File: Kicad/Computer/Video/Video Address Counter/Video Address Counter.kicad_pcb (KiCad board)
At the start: 2 copper layers, 26.7 x 90.2 mm, 5 parts, among them IC1 AP7365-33WG-7, J1 Conn_02x32_Counter_Clockwise

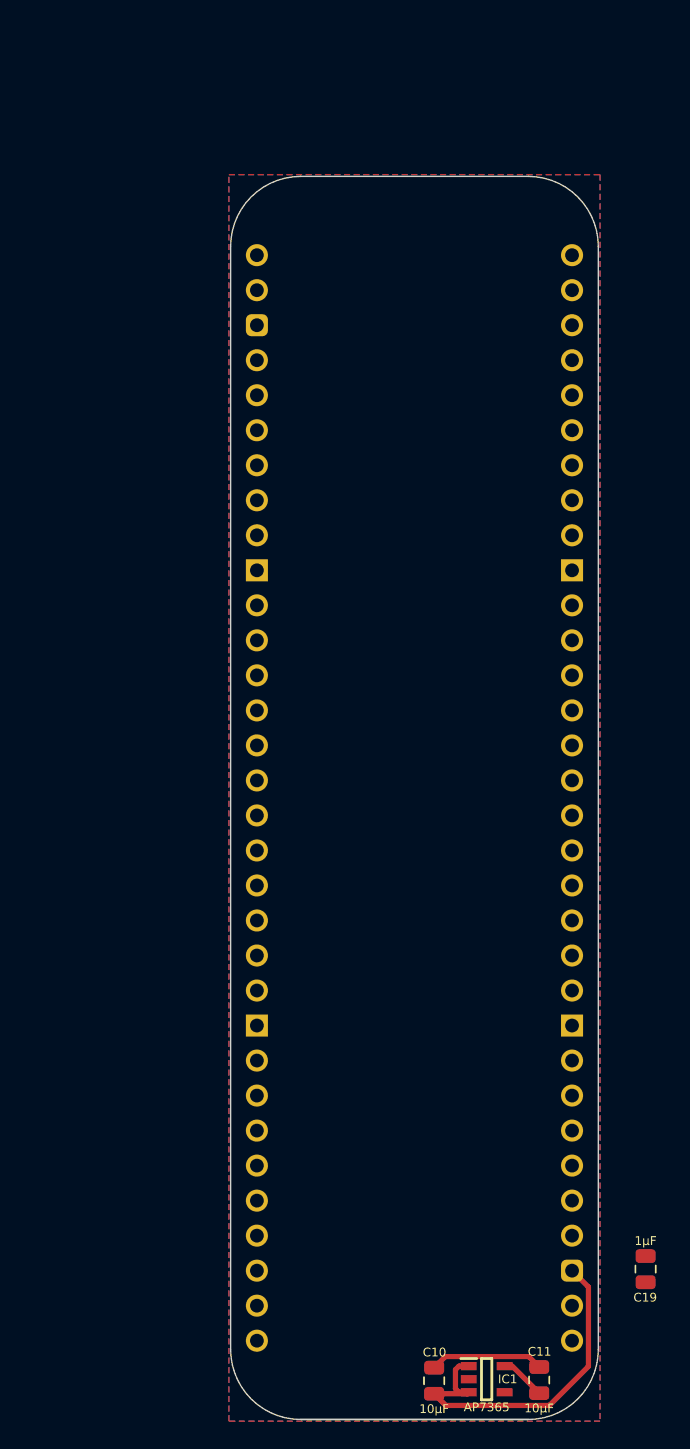
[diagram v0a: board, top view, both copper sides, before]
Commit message: Adding Video Address Counter.
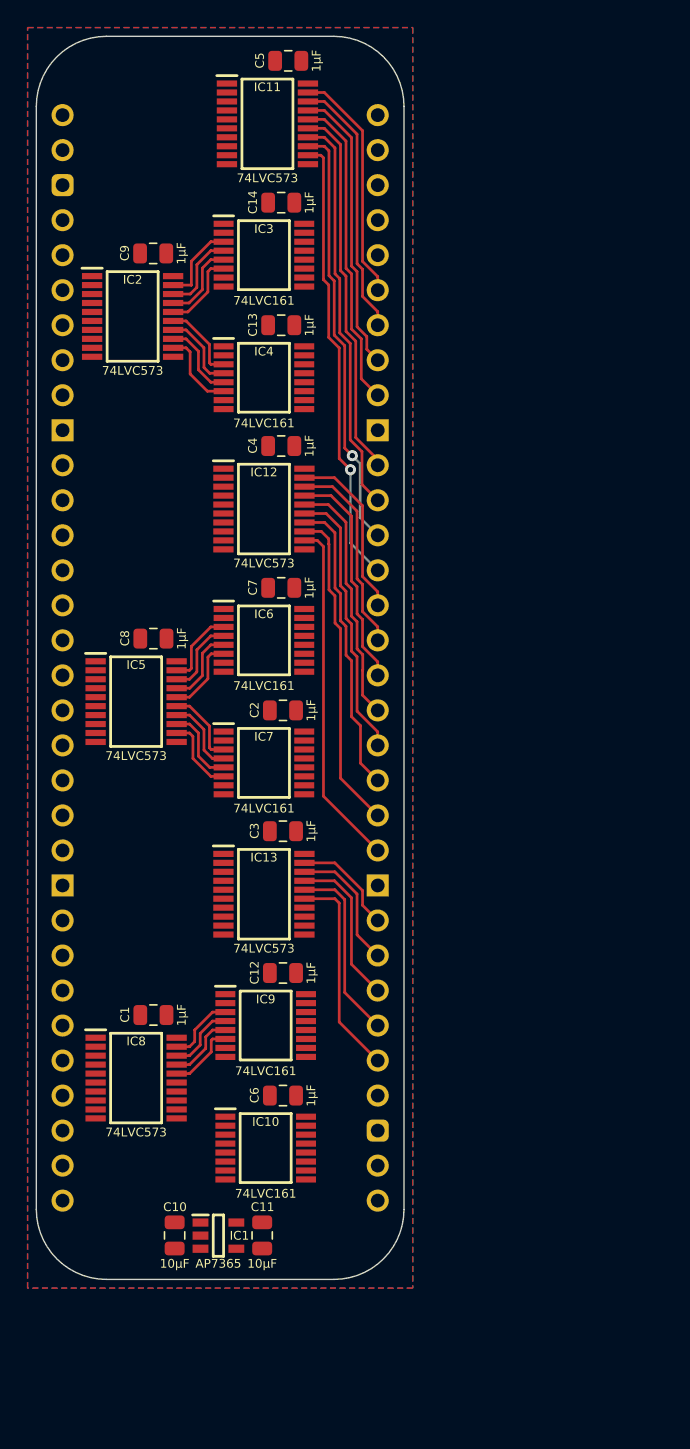
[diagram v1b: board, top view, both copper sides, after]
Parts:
- removed C19: 1μF, SamacSys_Parts:C_0805
- added C1: 1μF, SamacSys_Parts:C_0805, F.Cu at (81.4, 113.5)
- added C12: 1μF, SamacSys_Parts:C_0805, F.Cu at (90.8, 110.5)
- added C13: 1μF, SamacSys_Parts:C_0805, F.Cu at (90.7, 63.5)
- added C14: 1μF, SamacSys_Parts:C_0805, F.Cu at (90.7, 54.6)
- added C2: 1μF, SamacSys_Parts:C_0805, F.Cu at (90.8, 91.4)
- added C3: 1μF, SamacSys_Parts:C_0805, F.Cu at (90.8, 100.2)
- added C4: 1μF, SamacSys_Parts:C_0805, F.Cu at (90.7, 72.3)
- added C5: 1μF, SamacSys_Parts:C_0805, F.Cu at (91.2, 44.3)
- added C6: 1μF, SamacSys_Parts:C_0805, F.Cu at (90.8, 119.4)
- added C7: 1μF, SamacSys_Parts:C_0805, F.Cu at (90.7, 82.5)
- added C8: 1μF, SamacSys_Parts:C_0805, F.Cu at (81.4, 86.2)
- added C9: 1μF, SamacSys_Parts:C_0805, F.Cu at (81.4, 58.3)
- added IC10: 74LVC161PW,112, SamacSys_Parts:SOP65P640X110-16N, F.Cu at (89.5, 123.2)
- added IC11: 74LVC574APW,118, SamacSys_Parts:SOP65P640X110-20N, F.Cu at (89.7, 48.9)
- added IC12: 74LVC574APW,118, SamacSys_Parts:SOP65P640X110-20N, F.Cu at (89.4, 76.8)
- added IC13: 74LVC574APW,118, SamacSys_Parts:SOP65P640X110-20N, F.Cu at (89.4, 104.8)
- added IC2: 74LVC573APW,118, SamacSys_Parts:SOP65P640X110-20N, F.Cu at (79.9, 62.9)
- added IC3: 74LVC161PW,112, SamacSys_Parts:SOP65P640X110-16N, F.Cu at (89.4, 58.4)
- added IC4: 74LVC161PW,112, SamacSys_Parts:SOP65P640X110-16N, F.Cu at (89.4, 67.3)
- added IC5: 74LVC573APW,118, SamacSys_Parts:SOP65P640X110-20N, F.Cu at (80.1, 90.8)
- added IC6: 74LVC161PW,112, SamacSys_Parts:SOP65P640X110-16N, F.Cu at (89.4, 86.4)
- added IC7: 74LVC161PW,112, SamacSys_Parts:SOP65P640X110-16N, F.Cu at (89.4, 95.2)
- added IC8: 74LVC573APW,118, SamacSys_Parts:SOP65P640X110-20N, F.Cu at (80.1, 118.1)
- added IC9: 74LVC161PW,112, SamacSys_Parts:SOP65P640X110-16N, F.Cu at (89.5, 114.3)
- moved C11 22.7 mm to (89.3, 129.5)
- moved IC1 22.1 mm to (86.1, 129.5)
- moved C10 21.6 mm to (82.9, 129.5)
- moved J1 17.4 mm to (74.8, 48.3)
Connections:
- J1 pad 1: unconnected-(J1-Pin_1-Pad1) -> /~{Reset}
- J1 pad 11: unconnected-(J1-Pin_11-Pad11) -> /Pixel CLK
- J1 pad 12: unconnected-(J1-Pin_12-Pad12) -> /~{Pixel CLK}
- J1 pad 13: unconnected-(J1-Pin_13-Pad13) -> /L5
- J1 pad 14: unconnected-(J1-Pin_14-Pad14) -> /L6
- J1 pad 15: unconnected-(J1-Pin_15-Pad15) -> /L7
- J1 pad 16: unconnected-(J1-Pin_16-Pad16) -> /L8
- J1 pad 17: unconnected-(J1-Pin_17-Pad17) -> /L9
- J1 pad 18: unconnected-(J1-Pin_18-Pad18) -> /Latch High
- J1 pad 19: unconnected-(J1-Pin_19-Pad19) -> /L10
- J1 pad 2: unconnected-(J1-Pin_2-Pad2) -> /~{Horizontal Blank}
- J1 pad 20: unconnected-(J1-Pin_20-Pad20) -> /L11
- J1 pad 21: unconnected-(J1-Pin_21-Pad21) -> /L12
- J1 pad 22: unconnected-(J1-Pin_22-Pad22) -> /L13
- J1 pad 24: unconnected-(J1-Pin_24-Pad24) -> /L14
- J1 pad 25: unconnected-(J1-Pin_25-Pad25) -> /L15
- J1 pad 26: unconnected-(J1-Pin_26-Pad26) -> /Latch Bank
- J1 pad 27: unconnected-(J1-Pin_27-Pad27) -> /L16
- J1 pad 28: unconnected-(J1-Pin_28-Pad28) -> /L17
- J1 pad 29: unconnected-(J1-Pin_29-Pad29) -> /L18
- J1 pad 30: unconnected-(J1-Pin_30-Pad30) -> /L19
- J1 pad 31: unconnected-(J1-Pin_31-Pad31) -> /L20
- J1 pad 32: unconnected-(J1-Pin_32-Pad32) -> /Graphics Address ~{OE}
- J1 pad 37: unconnected-(J1-Pin_37-Pad37) -> /GA20
- J1 pad 38: unconnected-(J1-Pin_38-Pad38) -> /GA19
- J1 pad 39: unconnected-(J1-Pin_39-Pad39) -> /GA18
- J1 pad 4: unconnected-(J1-Pin_4-Pad4) -> /L0
- J1 pad 40: unconnected-(J1-Pin_40-Pad40) -> /GA17
- J1 pad 41: unconnected-(J1-Pin_41-Pad41) -> /GA16
- J1 pad 43: unconnected-(J1-Pin_43-Pad43) -> /GA15
- J1 pad 44: unconnected-(J1-Pin_44-Pad44) -> /GA14
- J1 pad 45: unconnected-(J1-Pin_45-Pad45) -> /GA13
- J1 pad 46: unconnected-(J1-Pin_46-Pad46) -> /GA12
- J1 pad 47: unconnected-(J1-Pin_47-Pad47) -> /GA11
- J1 pad 48: unconnected-(J1-Pin_48-Pad48) -> /GA10
- J1 pad 49: unconnected-(J1-Pin_49-Pad49) -> /GA9
- J1 pad 5: unconnected-(J1-Pin_5-Pad5) -> /L1
- J1 pad 50: unconnected-(J1-Pin_50-Pad50) -> /GA8
- J1 pad 51: unconnected-(J1-Pin_51-Pad51) -> /GA7
- J1 pad 52: unconnected-(J1-Pin_52-Pad52) -> /GA6
- J1 pad 53: unconnected-(J1-Pin_53-Pad53) -> /GA5
- J1 pad 54: unconnected-(J1-Pin_54-Pad54) -> /GA4
- J1 pad 56: unconnected-(J1-Pin_56-Pad56) -> /GA3
- J1 pad 57: unconnected-(J1-Pin_57-Pad57) -> /GA2
- J1 pad 58: unconnected-(J1-Pin_58-Pad58) -> /GA1
- J1 pad 59: unconnected-(J1-Pin_59-Pad59) -> /GA0
- J1 pad 6: unconnected-(J1-Pin_6-Pad6) -> /L2
- J1 pad 64: unconnected-(J1-Pin_64-Pad64) -> /Advance Pixel
- J1 pad 7: unconnected-(J1-Pin_7-Pad7) -> /L3
- J1 pad 8: unconnected-(J1-Pin_8-Pad8) -> /L4
- J1 pad 9: unconnected-(J1-Pin_9-Pad9) -> /Latch Low
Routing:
- net /GA7: track 0.00 -> 32.8 mm, vias 0 -> 1
- net /GA6: track 0.00 -> 31.0 mm, vias 0 -> 1
- net /GA5: track 0.00 -> 29.1 mm
- net /GA4: track 0.00 -> 27.2 mm
- net /5V: track 26.2 -> 0.00 mm
- net /GA15: track 0.00 -> 25.2 mm
- net /GA14: track 0.00 -> 23.5 mm
- net /GA3: track 0.00 -> 22.8 mm
- net /GA13: track 0.00 -> 21.8 mm
- net /GA2: track 0.00 -> 20.9 mm
- net /GA12: track 0.00 -> 19.9 mm
- net /GA1: track 0.00 -> 19.0 mm
- net /GA11: track 0.00 -> 18.2 mm
- net /GA0: track 0.00 -> 17.1 mm
- net /GA10: track 0.00 -> 16.4 mm
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
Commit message: Added Video Address Reader schematic and PCB.
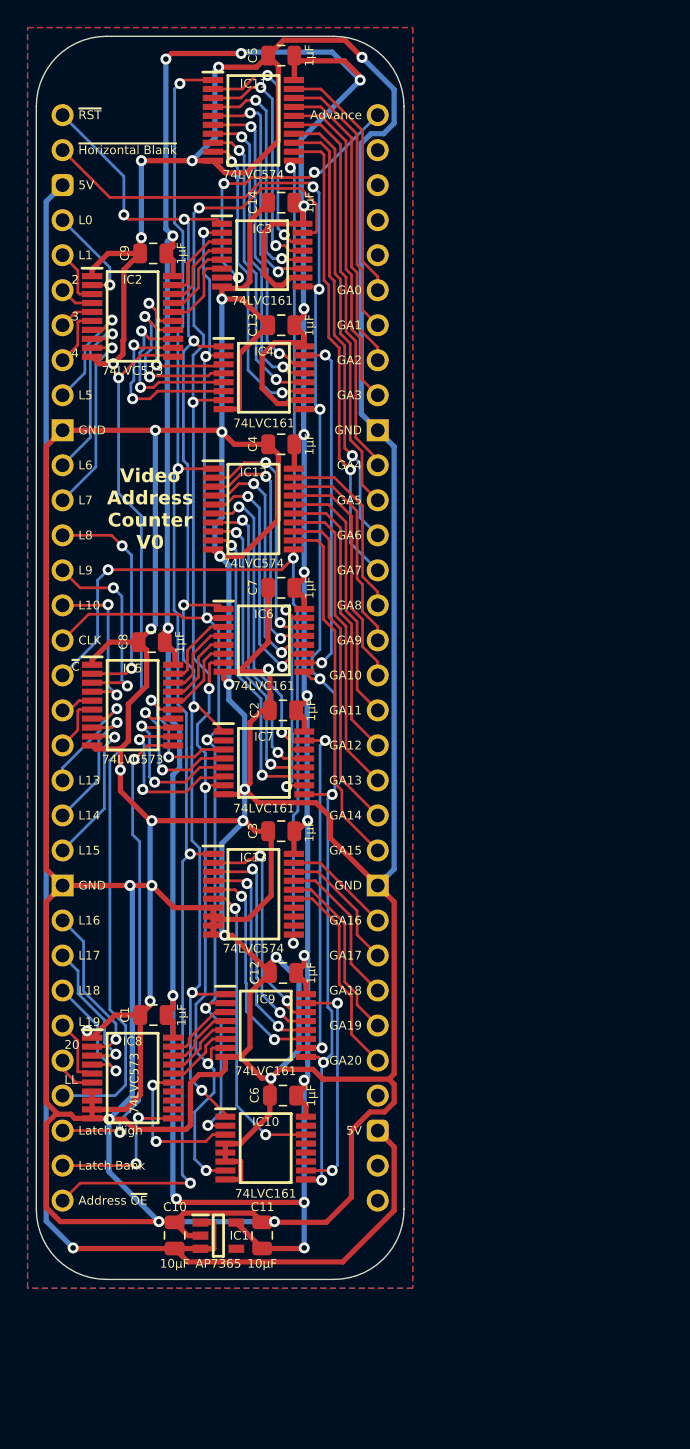
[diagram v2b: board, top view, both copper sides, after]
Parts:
- moved IC11 1.05 mm to (88.6, 48.6)
- moved IC12 0.76 mm to (88.6, 76.8)
- moved IC13 0.76 mm to (88.6, 104.8)
- moved C5 0.63 mm to (90.7, 43.9)
- moved IC5 0.36 mm to (79.9, 91.1)
- moved C8 0.28 mm to (81.3, 86.5)
- moved IC8 0.25 mm to (79.9, 118.1)
- moved C4 0.13 mm to (90.7, 72.1)
- moved C3 0.13 mm to (90.7, 100.2)
- moved IC3 0.13 mm to (89.3, 58.4)
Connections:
- net /GA0 renamed /A0
- net /GA1 renamed /A1
- net /GA10 renamed /A10
- net /GA11 renamed /A11
- net /GA12 renamed /A12
- net /GA13 renamed /A13
- net /GA14 renamed /A14
- net /GA15 renamed /A15
- net /GA16 renamed /A16
- net /GA17 renamed /A17
- net /GA18 renamed /A18
- net /GA19 renamed /A19
- net /GA2 renamed /A2
- net /GA20 renamed /A20
- net /GA3 renamed /A3
- net /GA4 renamed /A4
- net /GA5 renamed /A5
- net /GA6 renamed /A6
- net /GA7 renamed /A7
- net /GA8 renamed /A8
- net /GA9 renamed /A9
- net /Graphics Address ~{OE} renamed /Address ~{OE}
- J1 pad 11: /Pixel CLK -> /L6
- J1 pad 12: /~{Pixel CLK} -> /L7
- J1 pad 13: /L5 -> /L8
- J1 pad 14: /L6 -> /L9
- J1 pad 15: /L7 -> /L10
- J1 pad 16: /L8 -> /Pixel CLK
- J1 pad 17: /L9 -> /~{Pixel CLK}
- J1 pad 18: /Latch High -> /L11
- J1 pad 19: /L10 -> /L12
- J1 pad 20: /L11 -> /L13
- J1 pad 21: /L12 -> /L14
- J1 pad 22: /L13 -> /L15
- J1 pad 24: /L14 -> /L16
- J1 pad 25: /L15 -> /L17
- J1 pad 26: /Latch Bank -> /L18
- J1 pad 27: /L16 -> /L19
- J1 pad 28: /L17 -> /L20
- J1 pad 29: /L18 -> /Latch Low
- J1 pad 30: /L19 -> /Latch High
- J1 pad 31: /L20 -> /Latch Bank
- J1 pad 9: /Latch Low -> /L5
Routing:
- net /GND: track 0.00 -> 567.2 mm, vias 0 -> 27
- net /3.3V: track 0.00 -> 261.7 mm, vias 0 -> 17
- net /5V: track 0.00 -> 115.6 mm, vias 0 -> 1
- net /~{Horizontal Blank}: track 0.00 -> 102.5 mm, vias 0 -> 7
- net /Address ~{OE}: track 0.00 -> 97.9 mm, vias 0 -> 4
- net /TC_{0..3}: track 0.00 -> 96.1 mm, vias 0 -> 6
- net /~{Reset}: track 0.00 -> 95.1 mm, vias 0 -> 7
- net /Pixel CLK: track 0.00 -> 87.8 mm, vias 0 -> 6
- net /~{Pixel CLK}: track 0.00 -> 81.4 mm, vias 0 -> 4
- net /Latch Low: track 0.00 -> 62.8 mm, vias 0 -> 1
- net /Latch High: track 0.00 -> 35.4 mm, vias 0 -> 2
- net /TC_{4..7}: track 0.00 -> 25.6 mm, vias 0 -> 2
- net /TC_{12..15}: track 0.00 -> 25.2 mm, vias 0 -> 2
- net /C12: track 0.00 -> 22.4 mm, vias 0 -> 2
- net /C4: track 0.00 -> 22.3 mm, vias 0 -> 2
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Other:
- board text added: "2"
- board text added: "20"
- board text added: "3"
- board text added: "4"
- board text added: "5V"
- board text added: "Address ~{OE}"
- board text added: "Advance"
- board text added: "CLK"
- board text added: "GA0"
- board text added: "GA1"
- board text added: "GA10"
- board text added: "GA11"
- board text added: "GA12"
- board text added: "GA13"
- board text added: "GA14"
- board text added: "GA15"
- board text added: "GA16"
- board text added: "GA17"
- board text added: "GA18"
- board text added: "GA19"
- board text added: "GA2"
- board text added: "GA20"
- board text added: "GA3"
- board text added: "GA4"
- board text added: "GA5"
- board text added: "GA6"
- board text added: "GA7"
- board text added: "GA8"
- board text added: "GA9"
- board text added: "GND"
- board text added: "L0"
- board text added: "L1"
- board text added: "L10"
- board text added: "L13"
- board text added: "L14"
- board text added: "L15"
- board text added: "L16"
- board text added: "L17"
- board text added: "L18"
- board text added: "L19"
- board text added: "L5"
- board text added: "L6"
- board text added: "L7"
- board text added: "L8"
- board text added: "L9"
- board text added: "LL"
- board text added: "Latch Bank"
- board text added: "Latch High"
- board text added: "Video Address Counter V0"
- board text added: "~{C}"
- board text added: "~{Horizontal Blank}"
- board text added: "~{RST}"

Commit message: Still converting the Video Board.
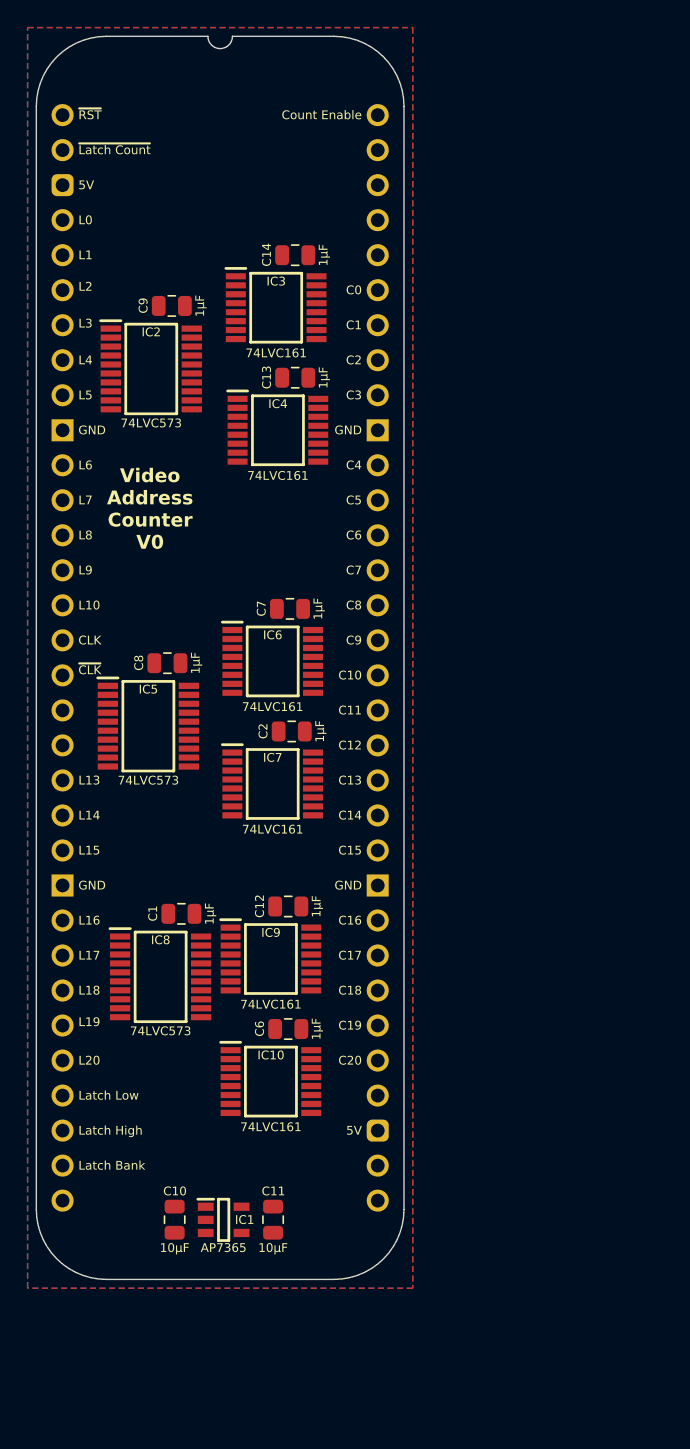
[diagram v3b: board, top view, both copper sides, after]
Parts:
- removed C3, C4, C5: 1μF, SamacSys_Parts:C_0805
- removed IC11, IC12, IC13: 74LVC574APW,118, SamacSys_Parts:SOP65P640X110-20N
- moved C1 7.62 mm to (83.4, 106.2)
- moved IC8 7.62 mm to (81.9, 110.8)
- moved C12 4.84 mm to (91.2, 105.7)
- moved C6 4.84 mm to (91.2, 114.6)
- moved IC10 4.84 mm to (89.9, 118.4)
- moved IC9 4.84 mm to (89.9, 109.5)
- moved C9 4.04 mm to (82.7, 62.1)
- moved IC2 4.04 mm to (81.2, 66.7)
- moved IC4 3.94 mm to (90.4, 71.1)
- moved C13 3.94 mm to (91.7, 67.3)
- moved C14 3.94 mm to (91.7, 58.4)
- moved IC3 3.94 mm to (90.3, 62.2)
- moved C8 1.91 mm to (82.4, 88.0)
- moved IC5 1.91 mm to (81.0, 92.6)
- moved IC6 1.65 mm to (90.0, 87.9)
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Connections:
- net /Advance Pixel renamed /Count Enable
- net /~{Horizontal Blank} renamed /~{Latch Count}
- J1 pad 32: /Address ~{OE} -> unconnected-(J1-Pin_32-Pad32)
- J1 pad 37: /A20 -> /C20
- J1 pad 38: /A19 -> /C19
- J1 pad 39: /A18 -> /C18
- J1 pad 40: /A17 -> /C17
- J1 pad 41: /A16 -> /C16
- J1 pad 43: /A15 -> /C15
- J1 pad 44: /A14 -> /C14
- J1 pad 45: /A13 -> /C13
- J1 pad 46: /A12 -> /C12
- J1 pad 47: /A11 -> /C11
- J1 pad 48: /A10 -> /C10
- J1 pad 49: /A9 -> /C9
- J1 pad 50: /A8 -> /C8
- J1 pad 51: /A7 -> /C7
- J1 pad 52: /A6 -> /C6
- J1 pad 53: /A5 -> /C5
- J1 pad 54: /A4 -> /C4
- J1 pad 56: /A3 -> /C3
- J1 pad 57: /A2 -> /C2
- J1 pad 58: /A1 -> /C1
- J1 pad 59: /A0 -> /C0
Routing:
- net /GND: track 567.2 -> 0.00 mm, vias 27 -> 0
- net /3.3V: track 261.7 -> 0.00 mm, vias 17 -> 0
- net /5V: track 115.6 -> 0.00 mm, vias 1 -> 0
- net /~{Latch Count}: track 102.5 -> 0.00 mm, vias 7 -> 0
- net /Address ~{OE}: track 97.9 -> 0.00 mm, vias 4 -> 0
- net /TC_{0..3}: track 96.1 -> 0.00 mm, vias 6 -> 0
- net /~{Reset}: track 95.1 -> 0.00 mm, vias 7 -> 0
- net /Pixel CLK: track 87.8 -> 0.00 mm, vias 6 -> 0
- net /~{Pixel CLK}: track 81.4 -> 0.00 mm, vias 4 -> 0
- net /Latch Low: track 62.8 -> 0.00 mm, vias 1 -> 0
- net /Latch High: track 35.4 -> 0.00 mm, vias 2 -> 0
- net /A7: track 34.0 -> 0.00 mm, vias 1 -> 0
- net /A6: track 32.1 -> 0.00 mm, vias 1 -> 0
- net /A5: track 30.2 -> 0.00 mm
- net /A4: track 27.9 -> 0.00 mm
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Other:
- outline, holes or cut-outs redrawn
- board text added: "C0"
- board text added: "C1"
- board text added: "C10"
- board text added: "C11"
- board text added: "C12"
- board text added: "C13"
- board text added: "C14"
- board text added: "C15"
- board text added: "C16"
- board text added: "C17"
- board text added: "C18"
- board text added: "C19"
- board text added: "C2"
- board text added: "C20"
- board text added: "C3"
- board text added: "C4"
- board text added: "C5"
- board text added: "C6"
- board text added: "C7"
- board text added: "C8"
- board text added: "C9"
- board text added: "Count Enable"
- board text added: "L2"
- board text added: "L20"
- board text added: "L3"
- board text added: "L4"
- board text added: "Latch Low"
- board text added: "~{CLK}"
- board text added: "~{Latch Count}"
- board text removed: "2"
- board text removed: "20"
- board text removed: "3"
- board text removed: "4"
- board text removed: "Address ~{OE}"
- board text removed: "Advance"
- board text removed: "GA0"
- board text removed: "GA1"
- board text removed: "GA10"
- board text removed: "GA11"
- board text removed: "GA12"
- board text removed: "GA13"
- board text removed: "GA14"
- board text removed: "GA15"
- board text removed: "GA16"
- board text removed: "GA17"
- board text removed: "GA18"
- board text removed: "GA19"
- board text removed: "GA2"
- board text removed: "GA20"
- board text removed: "GA3"
- board text removed: "GA4"
- board text removed: "GA5"
- board text removed: "GA6"
- board text removed: "GA7"
- board text removed: "GA8"
- board text removed: "GA9"
- board text removed: "LL"
- board text removed: "~{C}"
- board text removed: "~{Horizontal Blank}"
